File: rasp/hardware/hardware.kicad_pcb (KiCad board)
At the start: 2 copper layers, 65 x 69 mm, 43 parts, among them J10 Conn_01x02_Male, J11 Conn_01x02_Male, J12 Conn_01x02_Male, J13 Conn_01x02_Male, J14 Conn_01x02_Male, J15 Conn_01x02_Male, J16 Conn_01x02_Male, J17 Conn_01x02_Male, J18 Conn_01x02_Male, J19 Conn_01x02_Male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

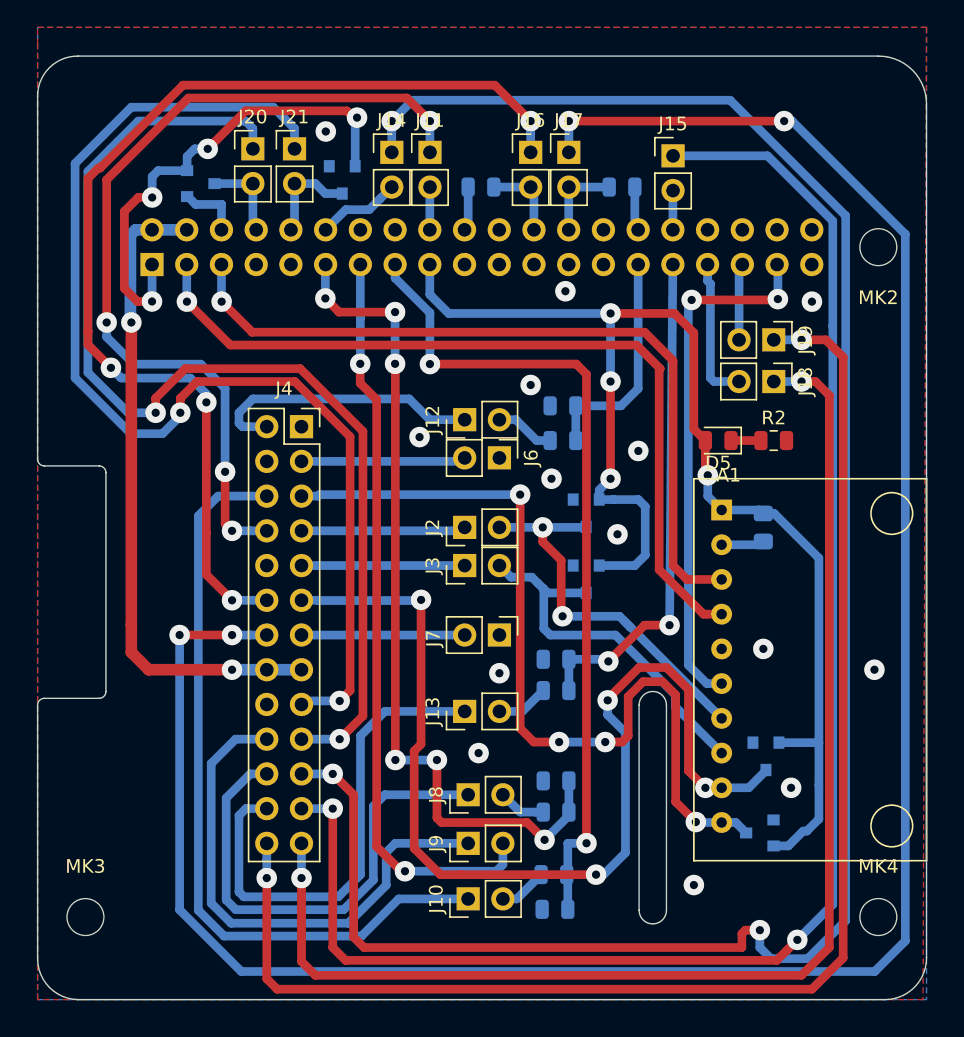
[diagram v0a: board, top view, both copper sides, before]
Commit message: Added silk labels
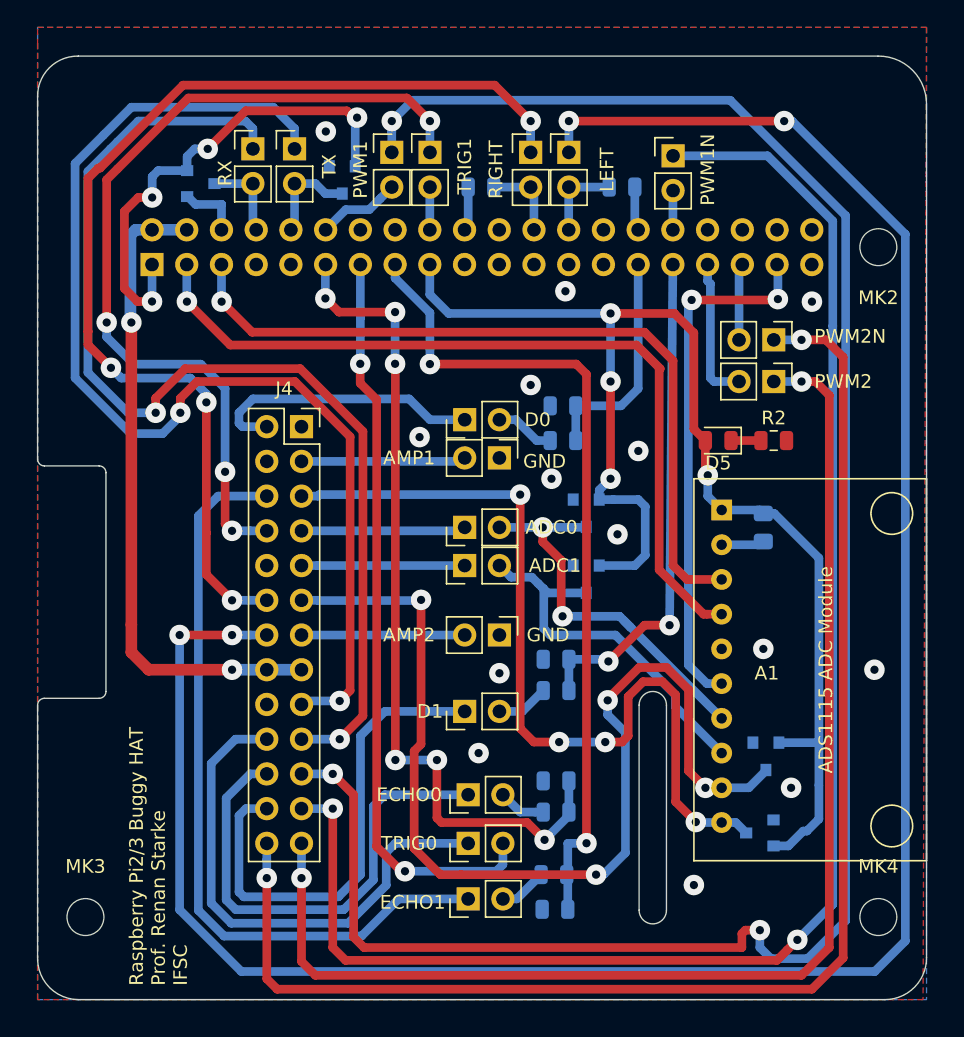
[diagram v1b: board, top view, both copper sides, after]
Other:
- board text added: "ADC0"
- board text added: "ADC1"
- board text added: "ADS1115 ADC Module"
- board text added: "AMP1"
- board text added: "AMP2"
- board text added: "D0"
- board text added: "D1"
- board text added: "ECHO0"
- board text added: "ECHO1"
- board text added: "GND"
- board text added: "LEFT"
- board text added: "PWM1"
- board text added: "PWM1N"
- board text added: "PWM2"
- board text added: "PWM2N"
- board text added: "RIGHT"
- board text added: "RX"
- board text added: "Raspberry Pi2/3 Buggy HAT Prof. Renan Starke IFSC"
- board text added: "TRIG0"
- board text added: "TRIG1"
- board text added: "TX"
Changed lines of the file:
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@@
   (general
     (thickness 1.6)
-    (drawings 39)
+    (drawings 61)
     (tracks 512)
     (zones 0)
@@
   (module Charleslabs_Parts:ADC1115_ADC_Module (layer F.Cu)
     (at 250.038 116.726)
-    (fp_text reference A1 (at 0.508 -2.54) (layer F.SilkS)
+    (fp_text reference A1 (at 3.302 11.938) (layer F.SilkS)
       (effects (font (size 1 1) (thickness 0.15)))
     )
@@
     (descr "Through hole straight pin header, 1x02, 2.54mm pitch, single row")
     (tags "Through hole pin header THT 1x02 2.54mm single row")
-    (fp_text reference J21 (at 0 -2.33) (layer F.SilkS)
+    (fp_text reference J21 (at 0 -2.33) (layer F.SilkS) hide
       (effects (font (size 1 1) (thickness 0.15)))
     )
@@
     (descr "Through hole straight pin header, 1x02, 2.54mm pitch, single row")
     (tags "Through hole pin header THT 1x02 2.54mm single row")
-    (fp_text reference J20 (at 0 -2.33) (layer F.SilkS)
+    (fp_text reference J20 (at 0 -2.33) (layer F.SilkS) hide
       (effects (font (size 1 1) (thickness 0.15)))
     )
@@
     (descr "Through hole straight pin header, 1x02, 2.54mm pitch, single row")
     (tags "Through hole pin header THT 1x02 2.54mm single row")
-    (fp_text reference J18 (at 0 -2.33 270) (layer F.SilkS)
+    (fp_text reference J18 (at 0 -2.33 270) (layer F.SilkS) hide
       (effects (font (size 1 1) (thickness 0.15)))
     )
@@
     (descr "Through hole straight pin header, 1x02, 2.54mm pitch, single row")
     (tags "Through hole pin header THT 1x02 2.54mm single row")
-    (fp_text reference J2 (at 0 -2.33 90) (layer F.SilkS)
+    (fp_text reference J2 (at 0 -2.33 90) (layer F.SilkS) hide
       (effects (font (size 1 1) (thickness 0.15)))
     )
@@
     (descr "Through hole straight pin header, 1x02, 2.54mm pitch, single row")
     (tags "Through hole pin header THT 1x02 2.54mm single row")
-    (fp_text reference J3 (at 0 -2.33 90) (layer F.SilkS)
+    (fp_text reference J3 (at 0 -2.33 90) (layer F.SilkS) hide
       (effects (font (size 1 1) (thickness 0.15)))
     )
@@
     (descr "Through hole straight pin header, 1x02, 2.54mm pitch, single row")
     (tags "Through hole pin header THT 1x02 2.54mm single row")
-    (fp_text reference J6 (at 0 -2.33 270) (layer F.SilkS)
+    (fp_text reference J6 (at 0 -2.33 270) (layer F.SilkS) hide
       (effects (font (size 1 1) (thickness 0.15)))
     )
@@
     (descr "Through hole straight pin header, 1x02, 2.54mm pitch, single row")
     (tags "Through hole pin header THT 1x02 2.54mm single row")
-    (fp_text reference J7 (at 0.254 4.826 270) (layer F.SilkS)
+    (fp_text reference J7 (at 0.254 4.826 270) (layer F.SilkS) hide
       (effects (font (size 1 1) (thickness 0.15)))
     )
@@
     (descr "Through hole straight pin header, 1x02, 2.54mm pitch, single row")
     (tags "Through hole pin header THT 1x02 2.54mm single row")
-    (fp_text reference J8 (at 0 -2.33 90) (layer F.SilkS)
+    (fp_text reference J8 (at 0 -2.33 90) (layer F.SilkS) hide
       (effects (font (size 1 1) (thickness 0.15)))
     )
@@
     (descr "Through hole straight pin header, 1x02, 2.54mm pitch, single row")
     (tags "Through hole pin header THT 1x02 2.54mm single row")
-    (fp_text reference J9 (at 0 -2.33 90) (layer F.SilkS)
+    (fp_text reference J9 (at 0 -2.33 90) (layer F.SilkS) hide
       (effects (font (size 1 1) (thickness 0.15)))
     )
@@
     (descr "Through hole straight pin header, 1x02, 2.54mm pitch, single row")
     (tags "Through hole pin header THT 1x02 2.54mm single row")
-    (fp_text reference J10 (at 0 -2.33 90) (layer F.SilkS)
+    (fp_text reference J10 (at 0 -2.33 90) (layer F.SilkS) hide
       (effects (font (size 1 1) (thickness 0.15)))
     )
@@
     (descr "Through hole straight pin header, 1x02, 2.54mm pitch, single row")
     (tags "Through hole pin header THT 1x02 2.54mm single row")
-    (fp_text reference J11 (at 0 -2.33) (layer F.SilkS)
+    (fp_text reference J11 (at 0 -2.33) (layer F.SilkS) hide
       (effects (font (size 1 1) (thickness 0.15)))
     )
@@
     (descr "Through hole straight pin header, 1x02, 2.54mm pitch, single row")
     (tags "Through hole pin header THT 1x02 2.54mm single row")
-    (fp_text reference J12 (at 0 -2.33 90) (layer F.SilkS)
+    (fp_text reference J12 (at 0 -2.33 90) (layer F.SilkS) hide
       (effects (font (size 1 1) (thickness 0.15)))
     )
@@
     (descr "Through hole straight pin header, 1x02, 2.54mm pitch, single row")
     (tags "Through hole pin header THT 1x02 2.54mm single row")
-    (fp_text reference J13 (at 0 -2.33 90) (layer F.SilkS)
+    (fp_text reference J13 (at 0 -2.33 90) (layer F.SilkS) hide
       (effects (font (size 1 1) (thickness 0.15)))
     )
@@
     (descr "Through hole straight pin header, 1x02, 2.54mm pitch, single row")
     (tags "Through hole pin header THT 1x02 2.54mm single row")
-    (fp_text reference J14 (at 0 -2.33) (layer F.SilkS)
+    (fp_text reference J14 (at 0 -2.33) (layer F.SilkS) hide
       (effects (font (size 1 1) (thickness 0.15)))
     )
@@
     (descr "Through hole straight pin header, 1x02, 2.54mm pitch, single row")
     (tags "Through hole pin header THT 1x02 2.54mm single row")
-    (fp_text reference J16 (at 0 -2.33) (layer F.SilkS)
+    (fp_text reference J16 (at 0 -2.33) (layer F.SilkS) hide
       (effects (font (size 1 1) (thickness 0.15)))
     )
@@
     (descr "Through hole straight pin header, 1x02, 2.54mm pitch, single row")
     (tags "Through hole pin header THT 1x02 2.54mm single row")
-    (fp_text reference J17 (at 0 -2.33) (layer F.SilkS)
+    (fp_text reference J17 (at 0 -2.33) (layer F.SilkS) hide
       (effects (font (size 1 1) (thickness 0.15)))
     )
@@
     (descr "Through hole straight pin header, 1x02, 2.54mm pitch, single row")
     (tags "Through hole pin header THT 1x02 2.54mm single row")
-    (fp_text reference J19 (at 0 -2.33 270) (layer F.SilkS)
+    (fp_text reference J19 (at 0 -2.33 270) (layer F.SilkS) hide
       (effects (font (size 1 1) (thickness 0.15)))
     )
@@
     (descr "Through hole straight pin header, 1x02, 2.54mm pitch, single row")
     (tags "Through hole pin header THT 1x02 2.54mm single row")
-    (fp_text reference J15 (at 0 -2.33) (layer F.SilkS)
+    (fp_text reference J15 (at 0 -2.33) (layer F.SilkS) hide
       (effects (font (size 1 1) (thickness 0.15)))
     )
@@
     (pad 1 np_thru_hole circle (at 0 0 180) (size 2.7 2.7) (drill 2.7) (layers *.Cu *.Mask))
   )
+  (gr_text "Raspberry Pi2/3 Buggy HAT\nProf. Renan Starke\nIFSC\n\n" (at 209.652 151.524 90) (layer F.SilkS)
+    (effects (font (size 1 1) (thickness 0.1)) (justify left))
+  )
+  (gr_text "ADS1115 ADC Module" (at 257.658 128.41 90) (layer F.SilkS)
+    (effects (font (size 1 1) (thickness 0.1)))
+  )
+  (gr_text GND (at 237.084 113.17) (layer F.SilkS)
+    (effects (font (size 1 1) (thickness 0.1)))
+  )
+  (gr_text ECHO1 (at 227.432 145.428) (layer F.SilkS)
+    (effects (font (size 1 1) (thickness 0.1)))
+  )
+  (gr_text TRIG0 (at 227.178 141.11) (layer F.SilkS)
+    (effects (font (size 1 1) (thickness 0.1)))
+  )
+  (gr_text ECHO0 (at 227.178 137.554) (layer F.SilkS)
+    (effects (font (size 1 1) (thickness 0.1)))
+  )
+  (gr_text D1 (at 228.702 131.458) (layer F.SilkS)
+    (effects (font (size 1 1) (thickness 0.1)))
+  )
+  (gr_text GND (at 237.338 125.87) (layer F.SilkS)
+    (effects (font (size 1 1) (thickness 0.1)))
+  )
+  (gr_text AMP2 (at 227.178 125.87) (layer F.SilkS)
+    (effects (font (size 1 1) (thickness 0.1)))
+  )
+  (gr_text ADC1 (at 237.846 120.79) (layer F.SilkS)
+    (effects (font (size 1 1) (thickness 0.1)))
+  )
+  (gr_text ADC0 (at 237.592 117.996) (layer F.SilkS)
+    (effects (font (size 1 1) (thickness 0.1)))
+  )
+  (gr_text AMP1 (at 227.178 112.916) (layer F.SilkS)
+    (effects (font (size 1 1) (thickness 0.1)))
+  )
+  (gr_text D0 (at 236.576 110.122) (layer F.SilkS)
+    (effects (font (size 1 1) (thickness 0.1)))
+  )
+  (gr_text PWM2 (at 258.928 107.328) (layer F.SilkS)
+    (effects (font (size 1 1) (thickness 0.1)))
+  )
+  (gr_text PWM2N (at 259.436 104.026) (layer F.SilkS)
+    (effects (font (size 1 1) (thickness 0.1)))
+  )
+  (gr_text RX (at 213.716 92.088 90) (layer F.SilkS)
+    (effects (font (size 1 1) (thickness 0.1)))
+  )
+  (gr_text TX (at 221.336 91.58 90) (layer F.SilkS)
+    (effects (font (size 1 1) (thickness 0.1)))
+  )
+  (gr_text PWM1 (at 223.622 91.834 90) (layer F.SilkS)
+    (effects (font (size 1 1) (thickness 0.1)))
+  )
+  (gr_text TRIG1 (at 231.242 91.58 90) (layer F.SilkS)
+    (effects (font (size 1 1) (thickness 0.1)))
+  )
+  (gr_text RIGHT (at 233.528 91.834 90) (layer F.SilkS)
+    (effects (font (size 1 1) (thickness 0.1)))
+  )
+  (gr_text LEFT (at 241.656 91.834 90) (layer F.SilkS)
+    (effects (font (size 1 1) (thickness 0.1)))
+  )
+  (gr_text PWM1N (at 249.022 91.834 90) (layer F.SilkS)
+    (effects (font (size 1 1) (thickness 0.1)))
+  )
   (gr_line (start 244 146) (end 244 131) (layer Edge.Cuts) (width 0.1))

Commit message: Added diode
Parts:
- added D8: D_Schottky, Diode_SMD:D_SMB, F.Cu at (207.6, 120.1)
- moved D7 0.80 mm to (222.2, 91.8)
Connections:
- J4 pad 15: +5V -> +5VP
- J4 pad 16: +5V -> +5VP
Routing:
- net +5V: track 47.8 -> 28.8 mm, vias 2 -> 1
- net +5VP: track 0.00 -> 16.6 mm
- net PWM1N: track 114.8 -> 115.9 mm
- net RXB: track 81.2 -> 82.3 mm
- net TXB: track 83.9 -> 85.0 mm
- net PWM1: track 146.2 -> 147.3 mm, vias 3 -> 5
- net GPIO18(GEN1)(PWM0): track 6.13 -> 6.96 mm
- net GND: vias 14 -> 16

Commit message: Added aligment holes
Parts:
- moved J18 0.65 mm to (253.8, 108.0)
- moved J19 0.65 mm to (253.8, 104.9)
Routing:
- net PWM2: track 93.4 -> 92.2 mm
- net PWM2N: track 102.9 -> 101.8 mm
- net +3V3: track 131.8 -> 131.3 mm
- net GND: vias 16 -> 19
- net (no net): vias 0 -> 4
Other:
- outline, holes or cut-outs redrawn

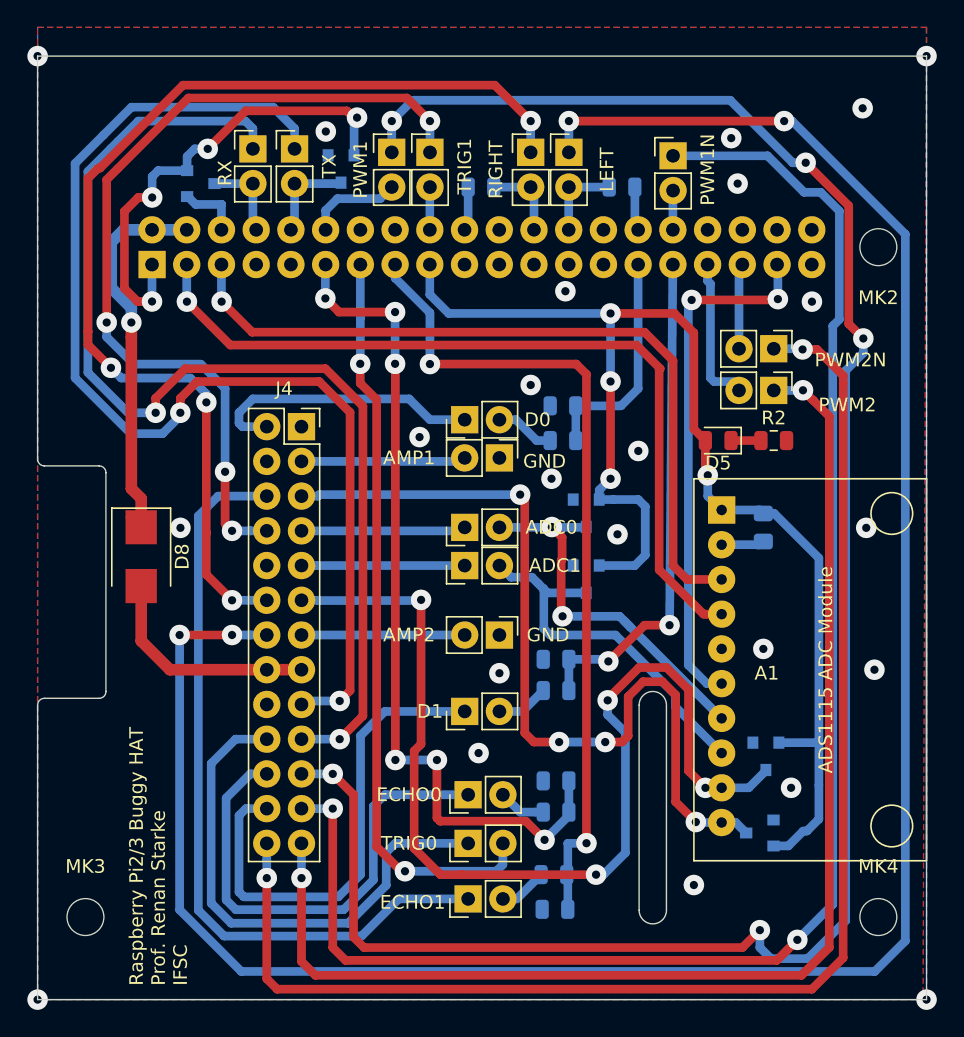
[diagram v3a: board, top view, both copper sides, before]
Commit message: Added i2c connector
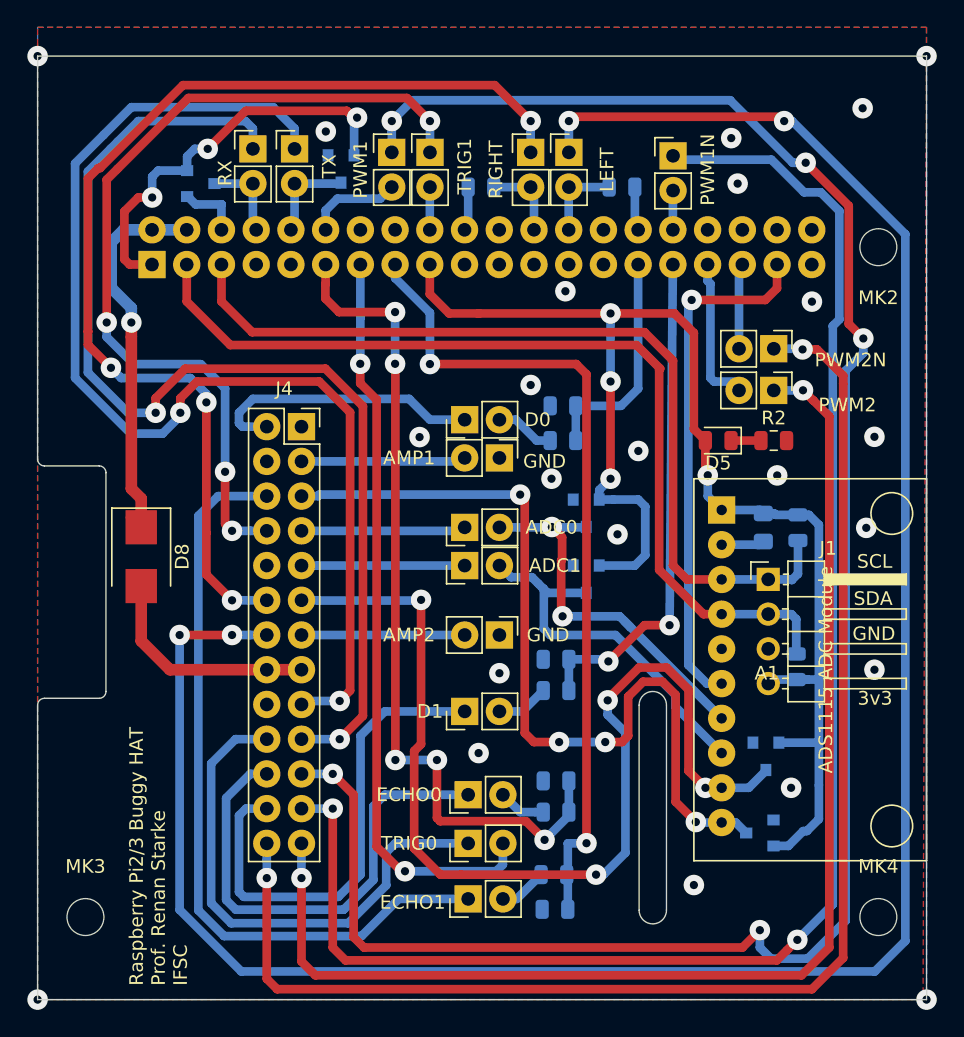
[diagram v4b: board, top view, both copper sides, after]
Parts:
- added J1: Conn_01x04_Male, Connector_PinHeader_2.54mm:PinHeader_1x04_P2.54mm_Horizontal, F.Cu at (253.4, 121.8)
- added R12: 2k2, Resistor_SMD:R_0805_2012Metric, B.Cu at (255.6, 118.0)
- added R13: 2k2, Resistor_SMD:R_0805_2012Metric, B.Cu at (255.5, 128.2)
- R10, R11, R3, R5, R8, R9: value 20K -> 18k
- R2: value R -> 820R
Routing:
- net GPIO3(SCL1): track 56.5 -> 64.7 mm, vias 1 -> 0
- net GPIO2(SDA1): track 60.0 -> 68.2 mm, vias 1 -> 0
- net GPIO26: track 38.7 -> 38.2 mm, vias 2 -> 1
- net +3V3: track 131.3 -> 131.5 mm, vias 8 -> 7
- net GPIO17(GEN0): vias 6 -> 5
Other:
- board text added: "3v3"
- board text added: "SCL"
- board text added: "SDA"

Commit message: Change 26vias connector
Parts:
- J4: footprint Connector_PinSocket_2.54mm:PinSocket_2x13_P2.54mm_Vertical -> Connector_IDC:IDC-Header_2x13_P2.54mm_Vertical
- moved J4 2.54 mm to (216.8, 110.6)
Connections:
- J4 pad 1: GND -> D0
- J4 pad 10: Net-(J4-Pad10) -> ADC1
- J4 pad 11: A2 -> R_TCRT
- J4 pad 12: R_TCRT -> A2
- J4 pad 13: AMP2 -> L_TCRT
- J4 pad 14: L_TCRT -> AMP2
- J4 pad 17: TXB -> Net-(J4-Pad17)
- J4 pad 18: Net-(J4-Pad18) -> TXB
- J4 pad 19: RXB -> Trig0
- J4 pad 2: D0 -> GND
- J4 pad 20: Trig0 -> RXB
- J4 pad 21: PWM1 -> Echo0
- J4 pad 22: Echo0 -> PWM1
- J4 pad 23: PWM1N -> D1
- J4 pad 24: D1 -> PWM1N
- J4 pad 25: PWM2 -> PWM2N
- J4 pad 26: PWM2N -> PWM2
- J4 pad 3: AMP1 -> GND
- J4 pad 4: GND -> AMP1
- J4 pad 5: A3 -> Echo1
- J4 pad 6: Echo1 -> A3
- J4 pad 7: ADC0 -> Trig1
- J4 pad 8: Trig1 -> ADC0
- J4 pad 9: ADC1 -> Net-(J4-Pad9)
